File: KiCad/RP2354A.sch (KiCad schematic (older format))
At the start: 1 part, among them U16 RP2354A

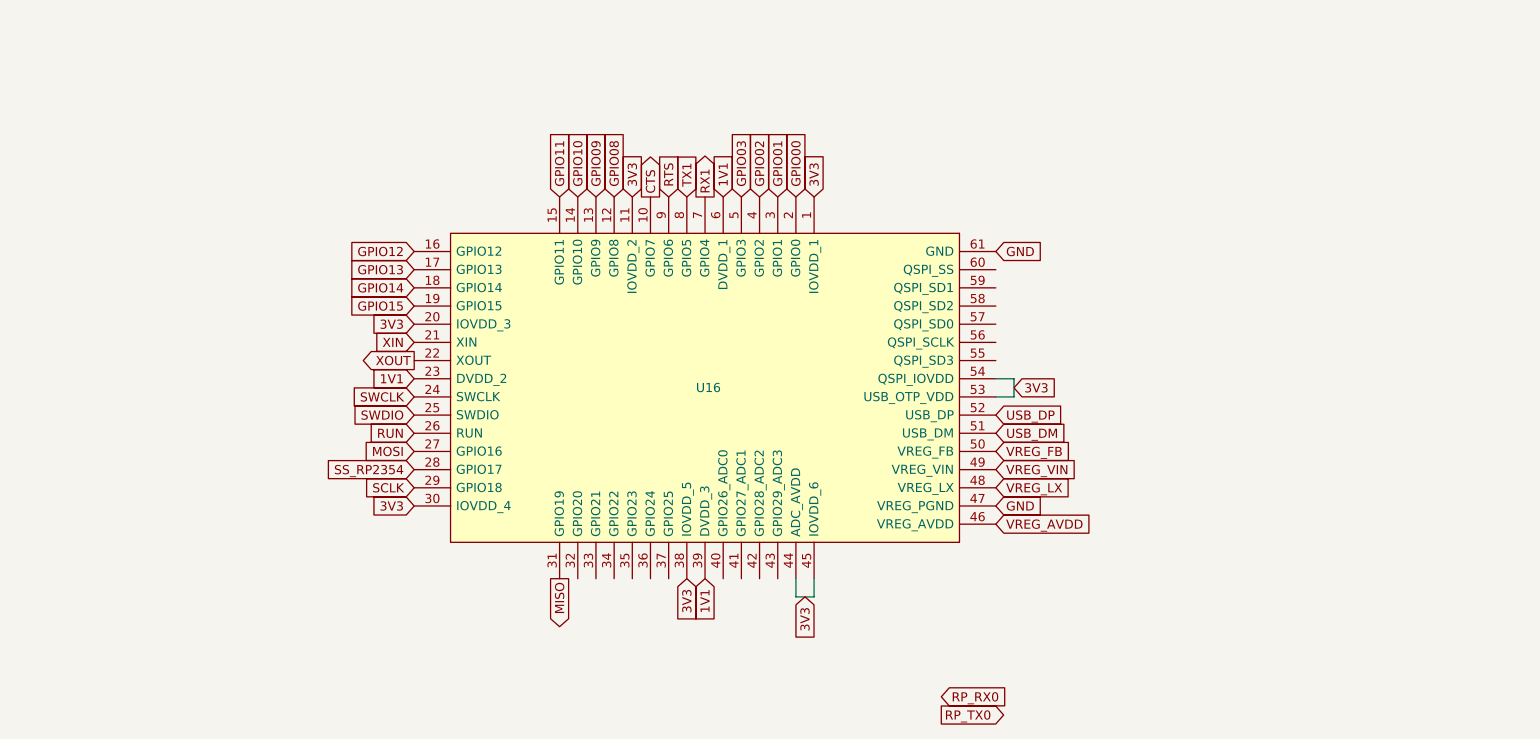
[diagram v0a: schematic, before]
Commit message: Add SPI header and rename some signals coming from the ESP32-C5
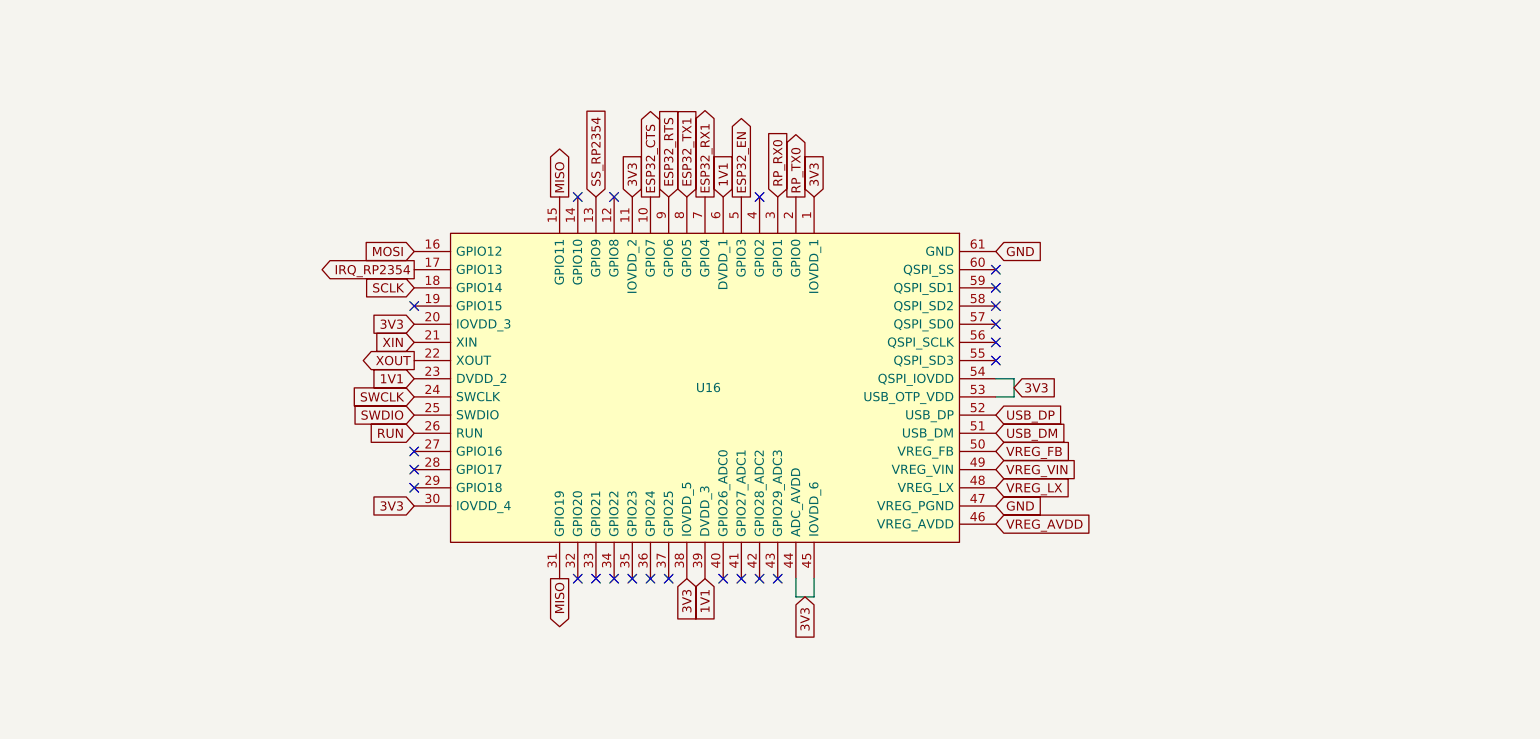
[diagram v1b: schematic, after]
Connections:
- net GPIO00 is gone; now on net RP_TX0: U16.2 (GPIO0)
- net GPIO01 is gone; now on net RP_RX0: U16.3 (GPIO1)
- net GPIO09 is gone; now on net SS_RP2354: U16.13 (GPIO9)
- net GPIO11 is gone; now on net MISO: U16.15 (GPIO11)
- net GPIO12 is gone; now on net MOSI: U16.16 (GPIO12)
- net GPIO14 is gone; now on net SCLK: U16.18 (GPIO14)
- net MOSI: no longer U16.27 (GPIO16)
- net SCLK: no longer U16.29 (GPIO18)
- net SS_RP2354: no longer U16.28 (GPIO17)
- net CTS renamed ESP32_CTS
- net GPIO02: no longer names the net of U16.4 (GPIO2)
- net GPIO03 renamed ESP32_EN
- net GPIO08: no longer names the net of U16.12 (GPIO8)
- net GPIO10: no longer names the net of U16.14 (GPIO10)
- net GPIO13 renamed IRQ_RP2354
- net GPIO15: no longer names the net of U16.19 (GPIO15)
- net RTS renamed ESP32_RTS
- net RX1 renamed ESP32_RX1
- net TX1 renamed ESP32_TX1
- no-connect marks 0 -> 23
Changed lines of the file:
@@
 Wire Wire Line
 	5800 4600 5900 4600
-Text GLabel 3700 4000 0    50   Input ~ 0
-SCLK
-Text GLabel 3700 3800 0    50   Input ~ 0
-MOSI
 Text GLabel 4500 4500 3    50   Output ~ 0
 MISO
-Text GLabel 3700 3900 0    50   Input ~ 0
+Text GLabel 5000 2400 1    50   Output ~ 0
+ESP32_CTS
+Text GLabel 5100 2400 1    50   Input ~ 0
+ESP32_RTS
+Text GLabel 5300 2400 1    50   Output ~ 0
+ESP32_RX1
+Text GLabel 5200 2400 1    50   Input ~ 0
+ESP32_TX1
+Text GLabel 3700 2700 0    50   Input ~ 0
+MOSI
+Text GLabel 4500 2400 1    50   Output ~ 0
+MISO
+Text GLabel 4700 2400 1    50   Input ~ 0
 SS_RP2354
-Text GLabel 3700 2700 0    50   Input ~ 0
-GPIO12
-Text GLabel 3700 2800 0    50   Input ~ 0
-GPIO13
 Text GLabel 3700 2900 0    50   Input ~ 0
-GPIO14
-Text GLabel 3700 3000 0    50   Input ~ 0
-GPIO15
-Text GLabel 4500 2400 1    50   Input ~ 0
-GPIO11
-Text GLabel 4600 2400 1    50   Input ~ 0
-GPIO10
-Text GLabel 4700 2400 1    50   Input ~ 0
-GPIO09
-Text GLabel 4800 2400 1    50   Input ~ 0
-GPIO08
-Text GLabel 5500 2400 1    50   Input ~ 0
-GPIO03
-Text GLabel 5600 2400 1    50   Input ~ 0
-GPIO02
+SCLK
+Text GLabel 3700 2800 0    50   Output ~ 0
+IRQ_RP2354
+NoConn ~ 4600 2400
+NoConn ~ 4800 2400
+NoConn ~ 3700 3000
+NoConn ~ 3700 3800
+NoConn ~ 3700 3900
+NoConn ~ 3700 4000
+Text GLabel 5800 2400 1    50   Output ~ 0
+RP_TX0
 Text GLabel 5700 2400 1    50   Input ~ 0
-GPIO01
-Text GLabel 5800 2400 1    50   Input ~ 0
-GPIO00
-Text GLabel 6600 5150 2    50   Input ~ 0
 RP_RX0
-Text GLabel 6600 5250 2    50   Output ~ 0
-RP_TX0
-Text GLabel 5000 2400 1    50   Output ~ 0
-CTS
-Text GLabel 5100 2400 1    50   Input ~ 0
-RTS
-Text GLabel 5300 2400 1    50   Output ~ 0
-RX1
-Text GLabel 5200 2400 1    50   Input ~ 0
-TX1
+NoConn ~ 4600 4500
+NoConn ~ 4700 4500
+NoConn ~ 4800 4500
+NoConn ~ 4900 4500
+NoConn ~ 5000 4500
+NoConn ~ 5100 4500
+NoConn ~ 5400 4500
+NoConn ~ 5500 4500
+NoConn ~ 5600 4500
+NoConn ~ 5700 4500
+NoConn ~ 6900 3300
+NoConn ~ 6900 3200
+NoConn ~ 6900 3100
+NoConn ~ 6900 3000
+NoConn ~ 6900 2900
+NoConn ~ 6900 2800
+NoConn ~ 5600 2400
+Text GLabel 5500 2400 1    50   Output ~ 0
+ESP32_EN
 $EndSCHEMATC

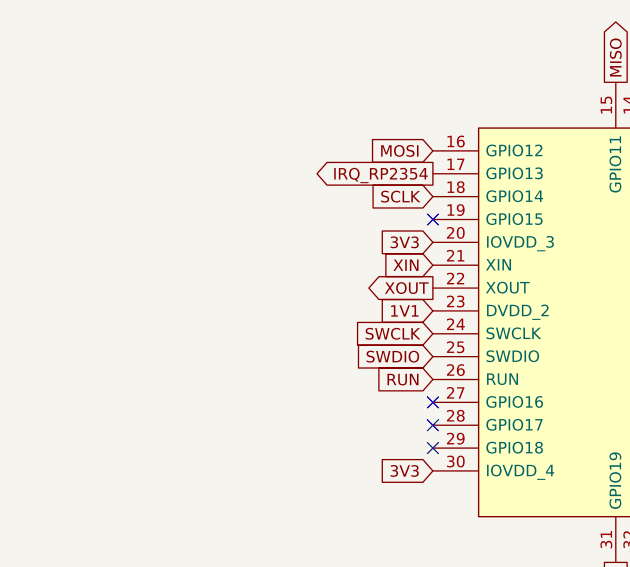
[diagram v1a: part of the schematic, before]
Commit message: Add 12 MHz crystal Y1 (Abracon ABM8-272-T3) for RP2354A (U16)
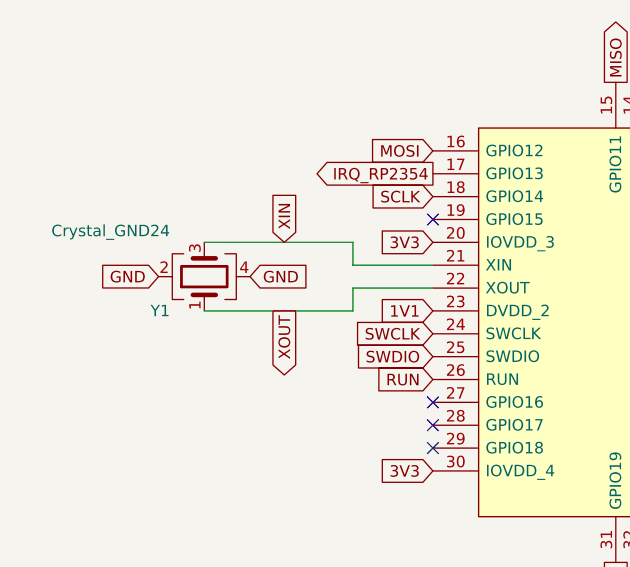
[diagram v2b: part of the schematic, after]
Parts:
- added Y1: Crystal_GND24, Crystal:Crystal_SMD_Abracon_ABM8G-4Pin_3.2x2.5mm, symbol Device:Crystal_GND24
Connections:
- net GND: now also Y1.2, Y1.4
- net XIN: now also Y1.3
- net XOUT: now also Y1.1
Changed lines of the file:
@@
 Text GLabel 5850 4600 3    50   Input ~ 0
 3V3
-Text GLabel 3700 3200 0    50   Input ~ 0
+Text GLabel 3050 3100 1    50   Input ~ 0
 XIN
-Text GLabel 3700 3300 0    50   Output ~ 0
+Text GLabel 3050 3400 3    50   Output ~ 0
 XOUT
 Text GLabel 3700 3400 0    50   Input ~ 0
@@
 Text GLabel 5500 2400 1    50   Output ~ 0
 ESP32_EN
+Text GLabel 2900 3250 2    50   Input ~ 0
+GND
+$Comp
+L Device:Crystal_GND24 Y1
+U 1 1 6B212228
+P 2700 3250
+F 0 "Y1" V 2550 3400 50  0000 L CNN
+F 1 "Crystal_GND24" V 2900 3400 50  0000 L CNN
+F 2 "Crystal:Crystal_SMD_Abracon_ABM8G-4Pin_3.2x2.5mm" H 2700 3250 50  0001 C CNN
+F 3 "~" H 2700 3250 50  0001 C CNN
+	1    2700 3250
+	0    -1   -1   0
+$EndComp
+Text GLabel 2500 3250 0    50   Input ~ 0
+GND
+Wire Wire Line
+	2700 3100 3350 3100
+Wire Wire Line
+	3350 3100 3350 3200
+Wire Wire Line
+	3350 3200 3700 3200
+Wire Wire Line
+	3700 3300 3350 3300
+Wire Wire Line
+	3350 3300 3350 3400
+Wire Wire Line
+	3350 3400 2700 3400
 $EndSCHEMATC

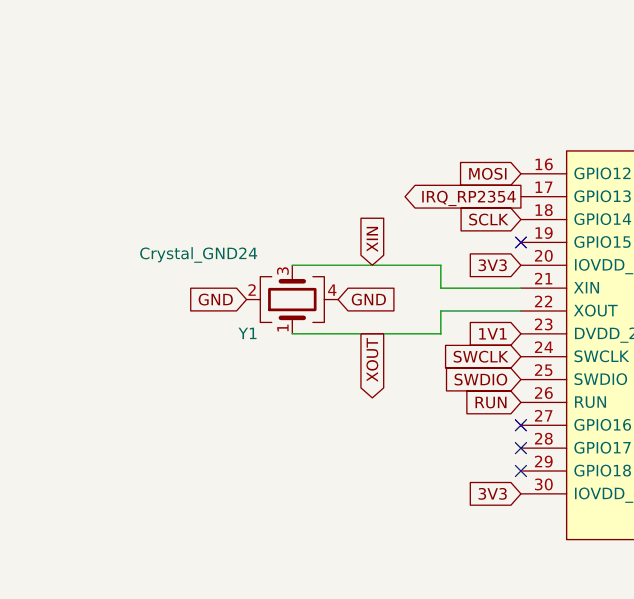
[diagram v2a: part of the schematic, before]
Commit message: Add 15pF caps and 1k resistor to Y1 (12 MHz crystal)
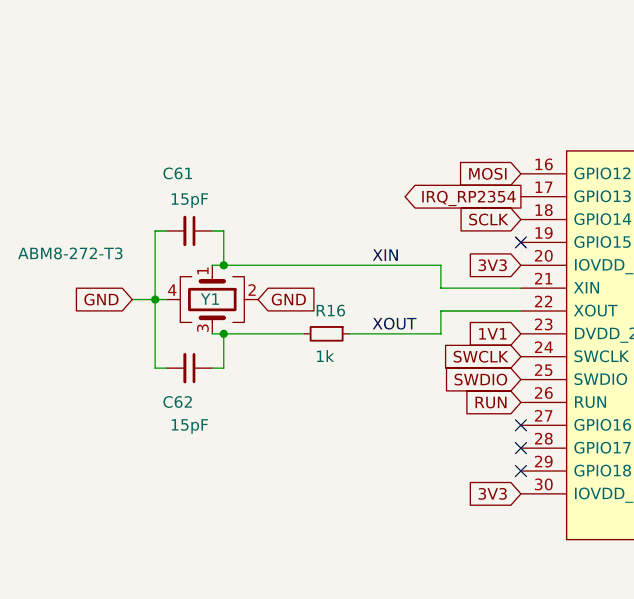
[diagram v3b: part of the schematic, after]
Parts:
- added C61, C62: 15pF, Capacitor_SMD:C_0603_1608Metric_Pad1.08x0.95mm_HandSolder, symbol Device:C_Small
- added R16: 1k, Resistor_SMD:R_0603_1608Metric_Pad0.98x0.95mm_HandSolder, symbol Device:R_Small
- Y1: value Crystal_GND24 -> ABM8-272-T3
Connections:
- net GND: now also C61.2, C62.2
- net XIN: now also Y1.1, C61.1; no longer Y1.3
- net XOUT: now also R16.1; no longer Y1.1
- new net: C62.1, R16.2, Y1.3
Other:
- moved on the sheet: Y1
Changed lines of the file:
@@
 Text GLabel 5850 4600 3    50   Input ~ 0
 3V3
-Text GLabel 3050 3100 1    50   Input ~ 0
-XIN
-Text GLabel 3050 3400 3    50   Output ~ 0
-XOUT
 Text GLabel 3700 3400 0    50   Input ~ 0
 1V1
@@
 Text GLabel 5500 2400 1    50   Output ~ 0
 ESP32_EN
-Text GLabel 2900 3250 2    50   Input ~ 0
+Text GLabel 2550 3250 2    50   Input ~ 0
 GND
 $Comp
 L Device:Crystal_GND24 Y1
 U 1 1 6B212228
-P 2700 3250
-F 0 "Y1" V 2550 3400 50  0000 L CNN
-F 1 "Crystal_GND24" V 2900 3400 50  0000 L CNN
-F 2 "Crystal:Crystal_SMD_Abracon_ABM8G-4Pin_3.2x2.5mm" H 2700 3250 50  0001 C CNN
-F 3 "~" H 2700 3250 50  0001 C CNN
-	1    2700 3250
-	0    -1   -1   0
+P 2350 3250
+F 0 "Y1" V 2350 3200 50  0000 L CNN
+F 1 "ABM8-272-T3" V 2150 2400 50  0000 L CNN
+F 2 "Crystal:Crystal_SMD_Abracon_ABM8G-4Pin_3.2x2.5mm" H 2350 3250 50  0001 C CNN
+F 3 "~" H 2350 3250 50  0001 C CNN
+	1    2350 3250
+	0    1    1    0
 $EndComp
-Text GLabel 2500 3250 0    50   Input ~ 0
+Text GLabel 2000 3250 0    50   Input ~ 0
 GND
 Wire Wire Line
-	2700 3100 3350 3100
+	2350 3100 2400 3100
 Wire Wire Line
 	3350 3100 3350 3200
@@
 Wire Wire Line
 	3350 3300 3350 3400
+$Comp
+L Device:C_Small C61
+U 1 1 6B2625A2
+P 2250 2950
+F 0 "C61" V 2000 2900 50  0000 C CNN
+F 1 "15pF" V 2112 2950 50  0000 C CNN
+F 2 "Capacitor_SMD:C_0603_1608Metric_Pad1.08x0.95mm_HandSolder" H 2250 2950 50  0001 C CNN
+F 3 "~" H 2250 2950 50  0001 C CNN
+	1    2250 2950
+	0    1    1    0
+$EndComp
+$Comp
+L Device:C_Small C62
+U 1 1 6B263398
+P 2250 3550
+F 0 "C62" V 2400 3500 50  0000 C CNN
+F 1 "15pF" V 2500 3550 50  0000 C CNN
+F 2 "Capacitor_SMD:C_0603_1608Metric_Pad1.08x0.95mm_HandSolder" H 2250 3550 50  0001 C CNN
+F 3 "~" H 2250 3550 50  0001 C CNN
+	1    2250 3550
+	0    1    1    0
+$EndComp
+Text Label 3050 3100 0    50   ~ 0
+XIN
+Text Label 3050 3400 0    50   ~ 0
+XOUT
 Wire Wire Line
-	3350 3400 2700 3400
+	2150 3250 2100 3250
+Wire Wire Line
+	2150 2950 2100 2950
+Wire Wire Line
+	2100 2950 2100 3250
+Connection ~ 2100 3250
+Wire Wire Line
+	2100 3250 2000 3250
+Wire Wire Line
+	2150 3550 2100 3550
+Wire Wire Line
+	2100 3550 2100 3250
+Wire Wire Line
+	2400 3400 2400 3550
+Wire Wire Line
+	2400 3550 2350 3550
+Wire Wire Line
+	2400 3400 2350 3400
+Wire Wire Line
+	2400 3100 2400 2950
+Wire Wire Line
+	2400 2950 2350 2950
+Connection ~ 2400 3100
+Wire Wire Line
+	2400 3100 3350 3100
+$Comp
+L Device:R_Small R?
+U 1 1 6B28DDCB
+P 2850 3400
+AR Path="/6B28DDCB" Ref="R?"  Part="1"
+AR Path="/6AFE5B10/6B28DDCB" Ref="R16"  Part="1"
+F 0 "R16" V 2750 3350 50  0000 L CNN
+F 1 "1k" V 2950 3350 50  0000 L CNN
+F 2 "Resistor_SMD:R_0603_1608Metric_Pad0.98x0.95mm_HandSolder" H 2850 3400 50  0001 C CNN
+F 3 "~" H 2850 3400 50  0001 C CNN
+	1    2850 3400
+	0    1    1    0
+$EndComp
+Wire Wire Line
+	2950 3400 3350 3400
+Wire Wire Line
+	2750 3400 2400 3400
+Connection ~ 2400 3400
 $EndSCHEMATC

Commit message: Add decoupling caps to RP2354A (U16)
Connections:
- net MISO: no longer U16.31 (GPIO19)
- no-connect marks 23 -> 24
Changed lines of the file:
@@
 Wire Wire Line
 	5800 4600 5900 4600
-Text GLabel 4500 4500 3    50   Output ~ 0
-MISO
 Text GLabel 5000 2400 1    50   Output ~ 0
 ESP32_CTS
@@
 	2750 3400 2400 3400
 Connection ~ 2400 3400
+NoConn ~ 4500 4500
 $EndSCHEMATC

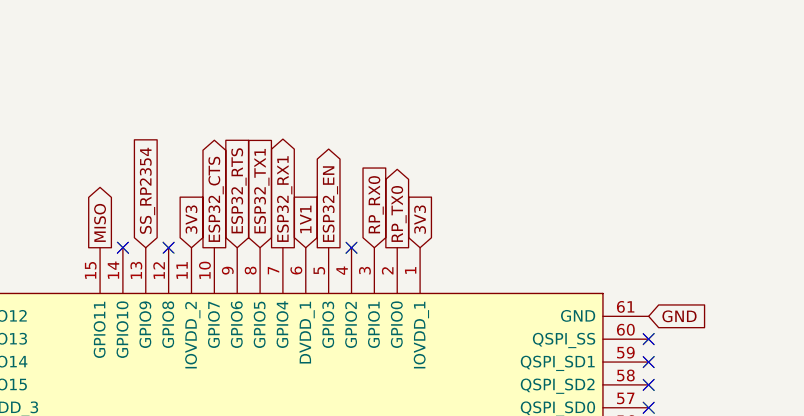
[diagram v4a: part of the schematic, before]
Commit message: Add UART0 two-pin-header for the RP2354A
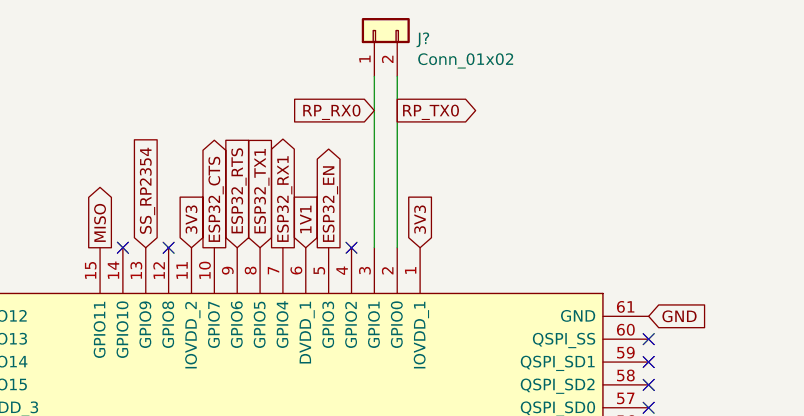
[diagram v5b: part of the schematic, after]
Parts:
- added J?: Conn_01x02, Connector_PinHeader_2.54mm:PinHeader_1x02_P2.54mm_Vertical, symbol Connector_Generic:Conn_01x02
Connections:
- net RP_RX0: now also J?.1 (Pin_1)
- net RP_TX0: now also J?.2 (Pin_2)
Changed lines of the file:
@@
 NoConn ~ 3700 3900
 NoConn ~ 3700 4000
-Text GLabel 5800 2400 1    50   Output ~ 0
+Text GLabel 5800 1800 2    50   Output ~ 0
 RP_TX0
-Text GLabel 5700 2400 1    50   Input ~ 0
+Text GLabel 5700 1800 0    50   Input ~ 0
 RP_RX0
 NoConn ~ 4600 4500
@@
 Connection ~ 2400 3400
 NoConn ~ 4500 4500
+$Comp
+L Connector_Generic:Conn_01x02 J?
+U 1 1 6ADBB844
+P 5700 1450
+F 0 "J?" V 5664 1262 50  0000 R CNN
+F 1 "Conn_01x02" V 5573 1262 50  0000 R CNN
+F 2 "Connector_PinHeader_2.54mm:PinHeader_1x02_P2.54mm_Vertical" H 5700 1450 50  0001 C CNN
+F 3 "~" H 5700 1450 50  0001 C CNN
+	1    5700 1450
+	0    -1   -1   0
+$EndComp
+Wire Wire Line
+	5700 1650 5700 2400
+Wire Wire Line
+	5800 1650 5800 2400
 $EndSCHEMATC

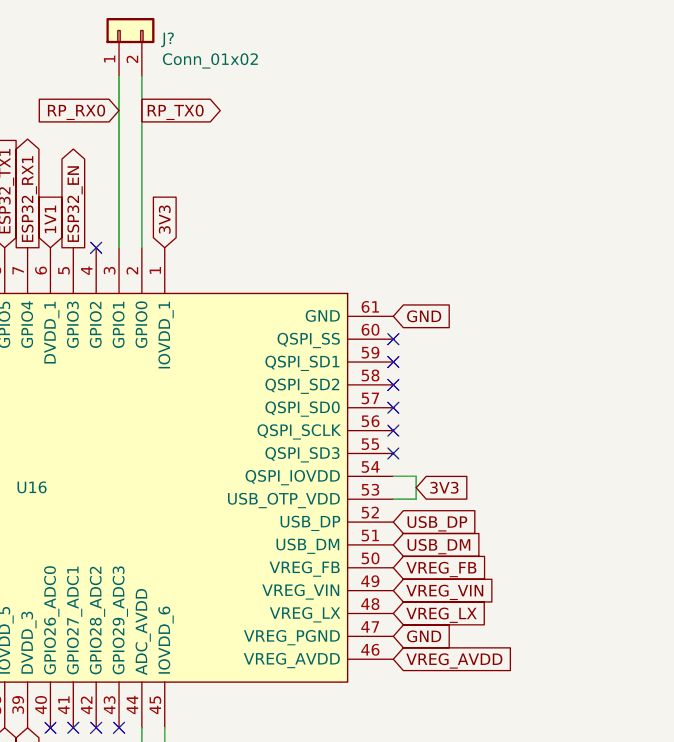
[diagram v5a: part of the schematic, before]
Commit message: Add two 27 Ohm series resistors on the USB_DP,USB_DM signals
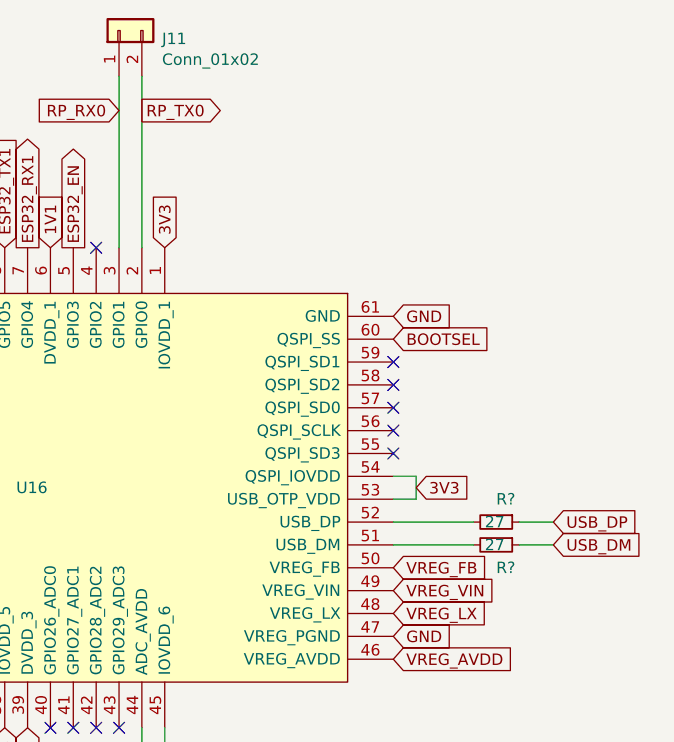
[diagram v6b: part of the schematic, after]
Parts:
- added R? (x2): 27, Resistor_SMD:R_0603_1608Metric_Pad0.98x0.95mm_HandSolder, symbol Device:R_Small
- gave numbers to parts that had none: 1
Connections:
- net USB_DM: now also R?.1; no longer U16.51 (USB_DM)
- net USB_DP: now also R?.1; no longer U16.52 (USB_DP)
- net BOOTSEL: now reaches U16.60 (QSPI_SS)
- new net: R?.2, U16.52 (USB_DP)
- new net: R?.2, U16.51 (USB_DM)
- no-connect marks 24 -> 23
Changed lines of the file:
@@
 Text GLabel 6900 2700 2    50   Input ~ 0
 GND
-Text GLabel 6900 3600 2    50   Input ~ 0
+Text GLabel 7600 3600 2    50   Input ~ 0
 USB_DP
-Text GLabel 6900 3700 2    50   Input ~ 0
+Text GLabel 7600 3700 2    50   Input ~ 0
 USB_DM
 Text GLabel 5900 2400 1    50   Input ~ 0
@@
 NoConn ~ 6900 3000
 NoConn ~ 6900 2900
-NoConn ~ 6900 2800
 NoConn ~ 5600 2400
 Text GLabel 5500 2400 1    50   Output ~ 0
@@
 NoConn ~ 4500 4500
 $Comp
-L Connector_Generic:Conn_01x02 J?
+L Connector_Generic:Conn_01x02 J11
 U 1 1 6ADBB844
 P 5700 1450
-F 0 "J?" V 5664 1262 50  0000 R CNN
+F 0 "J11" V 5664 1262 50  0000 R CNN
 F 1 "Conn_01x02" V 5573 1262 50  0000 R CNN
 F 2 "Connector_PinHeader_2.54mm:PinHeader_1x02_P2.54mm_Vertical" H 5700 1450 50  0001 C CNN
@@
 Wire Wire Line
 	5800 1650 5800 2400
+Text GLabel 6900 2800 2    50   Input ~ 0
+BOOTSEL
+$Comp
+L Device:R_Small R?
+U 1 1 6ADC9F07
+P 7350 3600
+AR Path="/6ADC9F07" Ref="R?"  Part="1"
+AR Path="/6AFE5B10/6ADC9F07" Ref="R?"  Part="1"
+F 0 "R?" V 7250 3600 50  0000 L CNN
+F 1 "27" V 7350 3550 50  0000 L CNN
+F 2 "Resistor_SMD:R_0603_1608Metric_Pad0.98x0.95mm_HandSolder" H 7350 3600 50  0001 C CNN
+F 3 "~" H 7350 3600 50  0001 C CNN
+	1    7350 3600
+	0    1    1    0
+$EndComp
+Wire Wire Line
+	6900 3600 7250 3600
+Wire Wire Line
+	7450 3600 7600 3600
+$Comp
+L Device:R_Small R?
+U 1 1 6ADD8B0E
+P 7350 3700
+AR Path="/6ADD8B0E" Ref="R?"  Part="1"
+AR Path="/6AFE5B10/6ADD8B0E" Ref="R?"  Part="1"
+F 0 "R?" V 7450 3700 50  0000 L CNN
+F 1 "27" V 7350 3650 50  0000 L CNN
+F 2 "Resistor_SMD:R_0603_1608Metric_Pad0.98x0.95mm_HandSolder" H 7350 3700 50  0001 C CNN
+F 3 "~" H 7350 3700 50  0001 C CNN
+	1    7350 3700
+	0    1    1    0
+$EndComp
+Wire Wire Line
+	6900 3700 7250 3700
+Wire Wire Line
+	7450 3700 7600 3700
 $EndSCHEMATC
